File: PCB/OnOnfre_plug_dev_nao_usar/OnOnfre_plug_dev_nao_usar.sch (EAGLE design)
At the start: 41 parts, among them IC4 HLW8012, J7 8p, Q3 2N7002, Q4 2N7002, U2 esp12

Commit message: Labels Fix
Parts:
- removed R5: VARISTORS07K230, varistor:VARISTORS07K230
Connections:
- net LINE_IN: now also U$2.AC2; no longer R5.1, U$2.AC1
- net NEUTRAL_IN: now also U$2.AC1; no longer R5.2, U$2.AC2
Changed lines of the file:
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@@
 <part name="AMS1117" library="SparkFun-IC-Power" library_urn="urn:adsk.eagle:library:526" deviceset="V_REG_LM1117" device="SOT223" package3d_urn="urn:adsk.eagle:package:39069/1" value="LM1117"/>
 <part name="FLASH" library="switches" deviceset="B3U" device="-1000P" value="B3U-1000P-2P-SMD"/>
-<part name="R5" library="varistor" library_urn="urn:adsk.eagle:library:410" deviceset="VARISTOR" device="S07K230" package3d_urn="urn:adsk.eagle:package:30547/1"/>
 <part name="J1" library="SparkFun-Connectors" library_urn="urn:adsk.eagle:library:513" deviceset="CONN_09" device="" package3d_urn="urn:adsk.eagle:package:38153/1"/>
 <part name="X1" library="con-wago-500" library_urn="urn:adsk.eagle:library:195" deviceset="W237-4" device="" package3d_urn="urn:adsk.eagle:package:10695/1"/>
@@
 <instance part="AMS1117" gate="G$1" x="259.08" y="147.32"/>
 <instance part="FLASH" gate="G$1" x="101.6" y="99.06"/>
-<instance part="R5" gate="G$1" x="231.14" y="167.64" smashed="yes" rot="R90">
-<attribute name="NAME" x="227.33" y="165.1" size="1.778" layer="95" rot="R90"/>
-<attribute name="VALUE" x="238.76" y="176.53" size="1.778" layer="96" rot="R180"/>
-</instance>
 <instance part="J1" gate="G$1" x="106.68" y="157.48"/>
 <instance part="X1" gate="-1" x="180.34" y="152.4"/>
@@
 <net name="NEUTRAL_IN" class="1">
 <segment>
-<pinref part="R5" gate="G$1" pin="2"/>
-<wire x1="231.14" y1="162.56" x2="220.98" y2="162.56" width="0.1524" layer="91"/>
-<label x="220.98" y="162.56" size="1.778" layer="95" rot="R180" xref="yes"/>
-<pinref part="U$2" gate="G$1" pin="AC2"/>
-<wire x1="241.3" y1="167.64" x2="238.76" y2="167.64" width="0.1524" layer="91"/>
-<wire x1="238.76" y1="167.64" x2="238.76" y2="162.56" width="0.1524" layer="91"/>
-<wire x1="238.76" y1="162.56" x2="231.14" y2="162.56" width="0.1524" layer="91"/>
-</segment>
-<segment>
 <label x="195.58" y="147.32" size="1.778" layer="95" xref="yes"/>
 <pinref part="X1" gate="-2" pin="KL"/>
@@
 <wire x1="185.42" y1="10.16" x2="185.42" y2="5.08" width="0.1524" layer="91"/>
 <label x="185.42" y="5.08" size="1.9304" layer="95" ratio="1" xref="yes"/>
+</segment>
+<segment>
+<pinref part="U$2" gate="G$1" pin="AC1"/>
+<wire x1="241.3" y1="172.72" x2="218.44" y2="172.72" width="0.1524" layer="91"/>
+<label x="218.44" y="172.72" size="1.778" layer="95" rot="R180" xref="yes"/>
 </segment>
 </net>
@@
 </segment>
 </net>
-<net name="N$12" class="0">
+<net name="N$12" class="1">
 <segment>
 <pinref part="R43" gate="G$1" pin="1"/>
@@
 </segment>
 </net>
-<net name="LINE_IN" class="1">
+<net name="LINE_IN" class="0">
 <segment>
 <label x="195.58" y="152.4" size="1.778" layer="95" xref="yes"/>
 <pinref part="X1" gate="-1" pin="KL"/>
 <wire x1="185.42" y1="152.4" x2="195.58" y2="152.4" width="0.1524" layer="91"/>
-</segment>
-<segment>
-<pinref part="U$2" gate="G$1" pin="AC1"/>
-<wire x1="241.3" y1="172.72" x2="231.14" y2="172.72" width="0.1524" layer="91"/>
-<pinref part="R5" gate="G$1" pin="1"/>
-<wire x1="231.14" y1="172.72" x2="218.44" y2="172.72" width="0.1524" layer="91"/>
-<junction x="231.14" y="172.72"/>
-<label x="218.44" y="172.72" size="1.778" layer="95" rot="R180" xref="yes"/>
 </segment>
 <segment>
@@
 <label x="182.88" y="96.52" size="1.9304" layer="95" ratio="1" rot="R180" xref="yes"/>
 </segment>
-</net>
+<segment>
+<wire x1="238.76" y1="162.56" x2="220.98" y2="162.56" width="0.1524" layer="91"/>
+<label x="220.98" y="162.56" size="1.778" layer="95" rot="R180" xref="yes"/>
+<pinref part="U$2" gate="G$1" pin="AC2"/>
+<wire x1="241.3" y1="167.64" x2="238.76" y2="167.64" width="0.1524" layer="91"/>
+<wire x1="238.76" y1="167.64" x2="238.76" y2="162.56" width="0.1524" layer="91"/>
+</segment>
+</net>

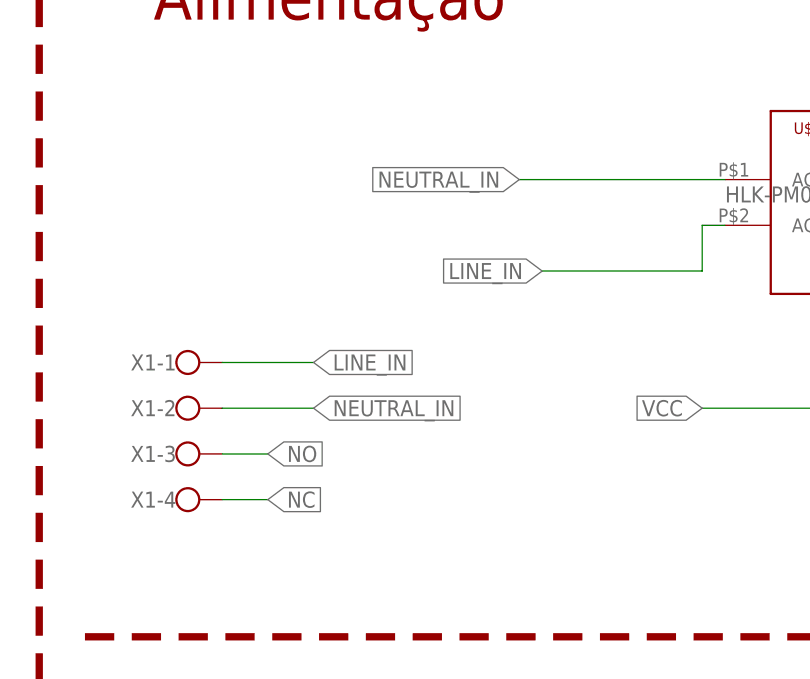
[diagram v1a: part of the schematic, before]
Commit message: remoção do OTA Arduino e adição de OTA via Web
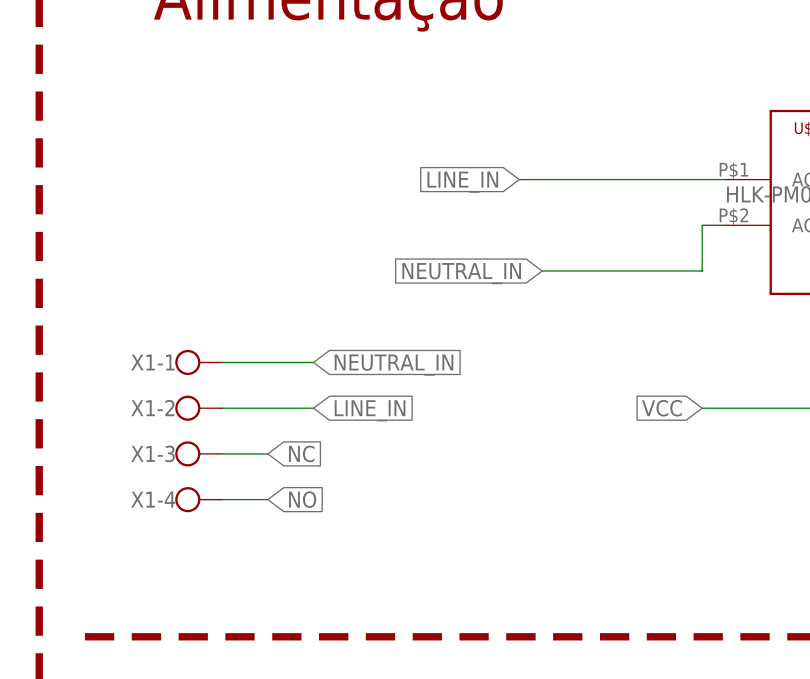
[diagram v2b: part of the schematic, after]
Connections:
- net LINE_IN: now also U$2.AC1, X1-2.KL; no longer U$2.AC2, X1-1.KL
- net NC: now also X1-3.KL; no longer X1-4.KL
- net NEUTRAL_IN: now also U$2.AC2, X1-1.KL; no longer U$2.AC1, X1-2.KL
- net NO: now also X1-4.KL; no longer X1-3.KL
